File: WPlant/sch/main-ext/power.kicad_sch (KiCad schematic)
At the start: 48 parts, among them J2 Battery, J3 Balance, J4 DE9_Receptacle, U2 AP64352SP-13, U3 AP64352SP-13, U4 AP64352SP-13, U6 AP2204R-5.0

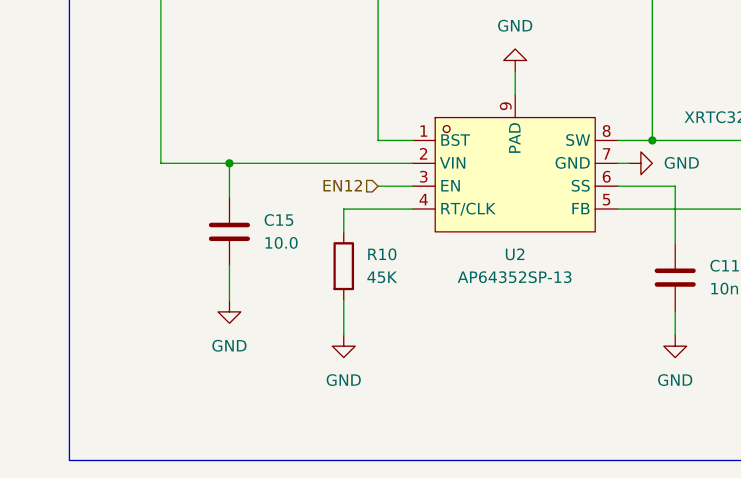
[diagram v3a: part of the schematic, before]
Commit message: Route of MainExt PCB done
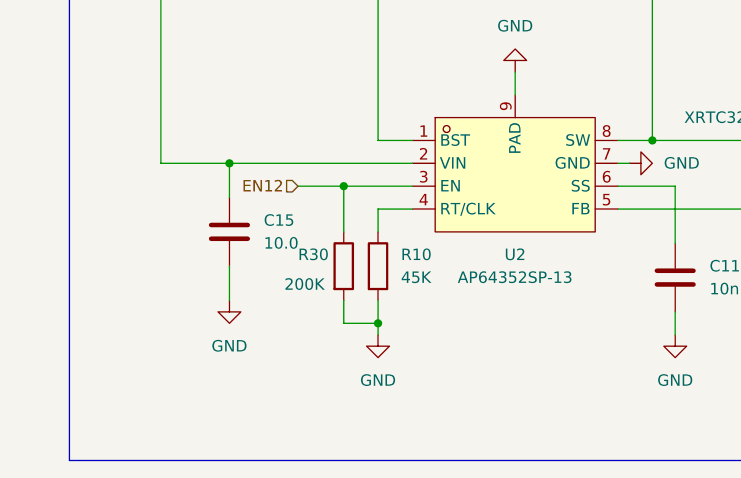
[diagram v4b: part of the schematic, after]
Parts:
- added R30: 200K, Resistor_SMD:R_0603_1608Metric_Pad0.98x0.95mm_HandSolder, symbol Device:R
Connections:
- net EN12: now also R30.1
- net GND: now also R30.2
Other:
- moved on the sheet: R10
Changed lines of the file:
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@@
 	)
 	(junction
+		(at 54.61 173.99)
+		(diameter 0)
+		(color 0 0 0 0)
+	)
+	(junction
 		(at 38.1 156.21)
 		(diameter 0)
@@
 	)
 	(junction
+		(at 50.8 158.75)
+		(diameter 0)
+		(color 0 0 0 0)
+	)
+	(junction
 		(at 107.95 41.91)
 		(diameter 0)
@@
 	(wire
 		(pts
+			(xy 50.8 171.45) (xy 50.8 173.99)
+		)
+		(stroke
+			(width 0)
+			(type default)
+		)
+	)
+	(wire
+		(pts
 			(xy 156.21 96.52) (xy 156.21 110.49)
 		)
@@
 	(wire
 		(pts
-			(xy 54.61 158.75) (xy 58.42 158.75)
+			(xy 45.72 158.75) (xy 50.8 158.75)
 		)
 		(stroke
@@
 	(wire
 		(pts
+			(xy 54.61 171.45) (xy 54.61 173.99)
+		)
+		(stroke
+			(width 0)
+			(type default)
+		)
+	)
+	(wire
+		(pts
 			(xy 50.8 101.6) (xy 58.42 101.6)
 		)
@@
 	(wire
 		(pts
-			(xy 50.8 163.83) (xy 50.8 161.29)
+			(xy 54.61 163.83) (xy 54.61 161.29)
 		)
 		(stroke
@@
 	(wire
 		(pts
+			(xy 50.8 158.75) (xy 50.8 163.83)
+		)
+		(stroke
+			(width 0)
+			(type default)
+		)
+	)
+	(wire
+		(pts
 			(xy 107.95 163.83) (xy 107.95 165.1)
 		)
@@
 	(wire
 		(pts
+			(xy 50.8 158.75) (xy 58.42 158.75)
+		)
+		(stroke
+			(width 0)
+			(type default)
+		)
+	)
+	(wire
+		(pts
 			(xy 252.73 33.02) (xy 256.54 33.02)
 		)
@@
 	(wire
 		(pts
+			(xy 50.8 173.99) (xy 54.61 173.99)
+		)
+		(stroke
+			(width 0)
+			(type default)
+		)
+	)
+	(wire
+		(pts
 			(xy 107.95 165.1) (xy 107.95 166.37)
 		)
@@
 	(wire
 		(pts
+			(xy 54.61 173.99) (xy 54.61 175.26)
+		)
+		(stroke
+			(width 0)
+			(type default)
+		)
+	)
+	(wire
+		(pts
 			(xy 102.87 41.91) (xy 107.95 41.91)
 		)
@@
 	(wire
 		(pts
-			(xy 50.8 161.29) (xy 58.42 161.29)
+			(xy 54.61 161.29) (xy 58.42 161.29)
 		)
 		(stroke
@@
 	(wire
 		(pts
-			(xy 50.8 171.45) (xy 50.8 175.26)
-		)
-		(stroke
-			(width 0)
-			(type default)
-		)
-	)
-	(wire
-		(pts
 			(xy 129.54 60.96) (xy 135.89 60.96)
 		)
@@
 	(hierarchical_label "EN12"
 		(shape input)
-		(at 54.61 158.75 180)
+		(at 45.72 158.75 180)
 		(fields_autoplaced yes)
 		(effects
@@
 	(symbol
 		(lib_id "Device:R")
-		(at 50.8 167.64 0)
+		(at 54.61 167.64 0)
 		(unit 1)
 		(exclude_from_sim no)
@@
 		(fields_autoplaced yes)
 		(property "Reference" "R10"
-			(at 53.34 166.3699 0)
+			(at 57.15 166.3699 0)
 			(effects
 				(font
@@
 		)
 		(property "Value" "45K"
-			(at 53.34 168.9099 0)
+			(at 57.15 168.9099 0)
 			(effects
 				(font
@@
 		)
 		(property "Footprint" "Resistor_SMD:R_0603_1608Metric_Pad0.98x0.95mm_HandSolder"
-			(at 49.022 167.64 90)
+			(at 52.832 167.64 90)
 			(effects
 				(font
@@
 		)
 		(property "Datasheet" "~"
-			(at 50.8 167.64 0)
+			(at 54.61 167.64 0)
 			(effects
 				(font
@@
 		)
 		(property "Description" "Resistor"
-			(at 50.8 167.64 0)
+			(at 54.61 167.64 0)
 			(effects
 				(font
@@
 	)
 	(symbol
+		(lib_id "Device:R")
+		(at 50.8 167.64 0)
+		(unit 1)
+		(exclude_from_sim no)
+		(in_bom yes)
+		(on_board yes)
+		(dnp no)
+		(property "Reference" "R30"
+			(at 45.72 166.37 0)
+			(effects
+				(font
+					(size 1.27 1.27)
+				)
+				(justify left)
+			)
+		)
+		(property "Value" "200K"
+			(at 44.196 169.672 0)
+			(effects
+				(font
+					(size 1.27 1.27)
+				)
+				(justify left)
+			)
+		)
+		(property "Footprint" "Resistor_SMD:R_0603_1608Metric_Pad0.98x0.95mm_HandSolder"
+			(at 49.022 167.64 90)
+			(effects
+				(font
+					(size 1.27 1.27)
+				)
+				(hide yes)
+			)
+		)
+		(property "Datasheet" "~"
+			(at 50.8 167.64 0)
+			(effects
+				(font
+					(size 1.27 1.27)
+				)
+				(hide yes)
+			)
+		)
+		(property "Description" "Resistor"
+			(at 50.8 167.64 0)
+			(effects
+				(font
+					(size 1.27 1.27)
+				)
+				(hide yes)
+			)
+		)
+		(pin "1"
+		)
+		(pin "2"
+		)
+		(instances
+			(project "main-ext"
+				(path "/71bd3f7f-463d-4a2c-bec7-ca56c2fe6cec/e5010fd4-921a-4703-b472-3554db39dd22"
+					(reference "R30")
+					(unit 1)
+				)
+			)
+		)
+	)
+	(symbol
 		(lib_id "power:GND")
 		(at 107.95 120.65 0)
@@
 	(symbol
 		(lib_id "power:GND")
-		(at 50.8 175.26 0)
+		(at 54.61 175.26 0)
 		(unit 1)
 		(exclude_from_sim no)
@@
 		(fields_autoplaced yes)
 		(property "Reference" "#PWR020"
-			(at 50.8 181.61 0)
+			(at 54.61 181.61 0)
 			(effects
 				(font
@@
 		)
 		(property "Value" "GND"
-			(at 50.8 180.34 0)
+			(at 54.61 180.34 0)
 			(effects
 				(font
@@
 		)
 		(property "Footprint" ""
-			(at 50.8 175.26 0)
+			(at 54.61 175.26 0)
 			(effects
 				(font
@@
 		)
 		(property "Datasheet" ""
-			(at 50.8 175.26 0)
+			(at 54.61 175.26 0)
 			(effects
 				(font
@@
 		)
 		(property "Description" "Power symbol creates a global label with name \"GND\" , ground"
-			(at 50.8 175.26 0)
+			(at 54.61 175.26 0)
 			(effects
 				(font

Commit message: Update WP Sch (sheets titles, replaced wires by bus, update components values)
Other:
- title: Power module -> Power module (WPMain Ext)
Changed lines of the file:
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@@
 	(paper "A4")
 	(title_block
-		(title "Power module")
+		(title "Power module (WPMain Ext)")
+		(date "2026-02-05")
 		(company "RoboWay")
 	)
